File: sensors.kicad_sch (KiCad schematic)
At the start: 0 parts

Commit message: feat: setup encoder reading
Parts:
- added C30, C31: 10n, Capacitor_SMD:C_0603_1608Metric, symbol Device:C
- added C32, C33: 100n, Capacitor_SMD:C_0603_1608Metric, symbol Device:C
- added C34: 1n, Capacitor_SMD:C_0603_1608Metric, symbol Device:C
- added R13, R14: 120R, Resistor_SMD:R_0603_1608Metric, symbol Device:R
- added R15, R16, R17, R18: R, symbol Device:R
- added U2: ACS724LLCTR-10AB-T, Package_SO:SOIC-8_3.9x4.9mm_P1.27mm, symbol Sensor_Current:ACS724xLCTR-10AB
- added U3: UA9637A, Package_SO:SOIC-8_3.9x4.9mm_P1.27mm, symbol Eagle_Main:UA9637A
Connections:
- new net: C30.1, R13.1
- new net: R15.1, U3.2 (OUT1)
- new net: C31.1, R14.1
- new net: R16.1, U3.3 (OUT2)
- new net: U2.1 (IP+), U2.2 (IP+)
- new net: U2.3 (IP-), U2.4 (IP-)
- new net: C34.1, U2.6 (FILTER)
- new net +5V: C32.1, C33.1, U2.8 (VCC), U3.1 (VCC)
- new net GND: C32.2, C33.2, C34.2, R17.1, R18.2, U2.5 (GND), U3.4 (GND)
- new net M1_A: R15.2
- new net M1_A+: R13.2, U3.8 (IN1+)
- new net M1_A-: C30.2, U3.7 (IN1-)
- new net M1_B: R16.2, R17.2, R18.1
- new net M1_B+: R14.2, U3.6 (IN2+)
- new net M1_B-: C31.2, U3.5 (IN2-)
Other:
- note added: "MOTOR 1 - X axis"

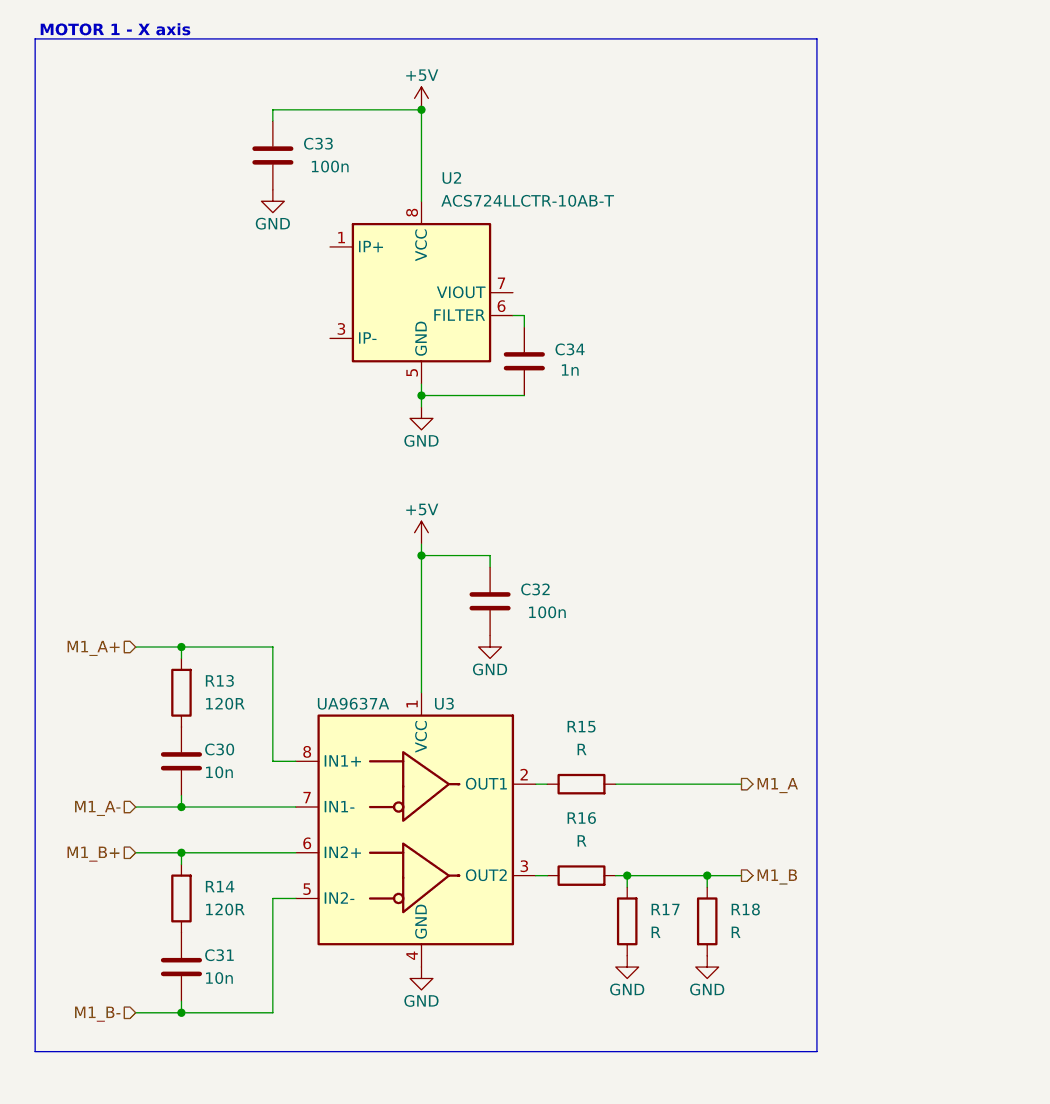
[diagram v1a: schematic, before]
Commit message: feat: RC filter on encoder data
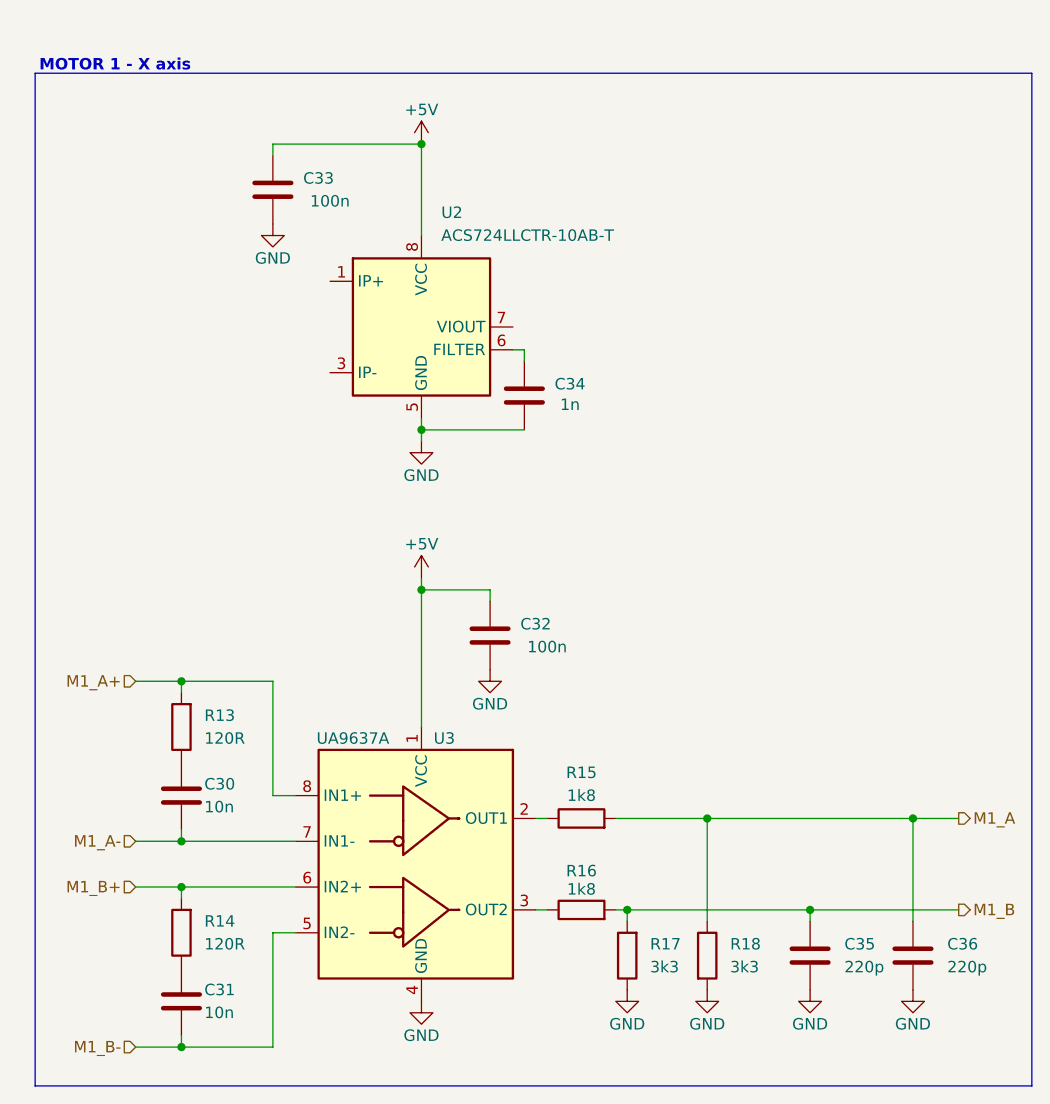
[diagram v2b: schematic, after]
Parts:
- added C35, C36: 220p, symbol Device:C
- R15, R16: value R -> 1k8
- R17, R18: value R -> 3k3
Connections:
- net GND: now also C35.2, C36.2
- net M1_A: now also R18.1, C36.1
- net M1_B: now also C35.1; no longer R18.1
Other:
- moved on the sheet: C30, C31, C32, C33, C34, R13, R14, R15, R16, R17, R18, U2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

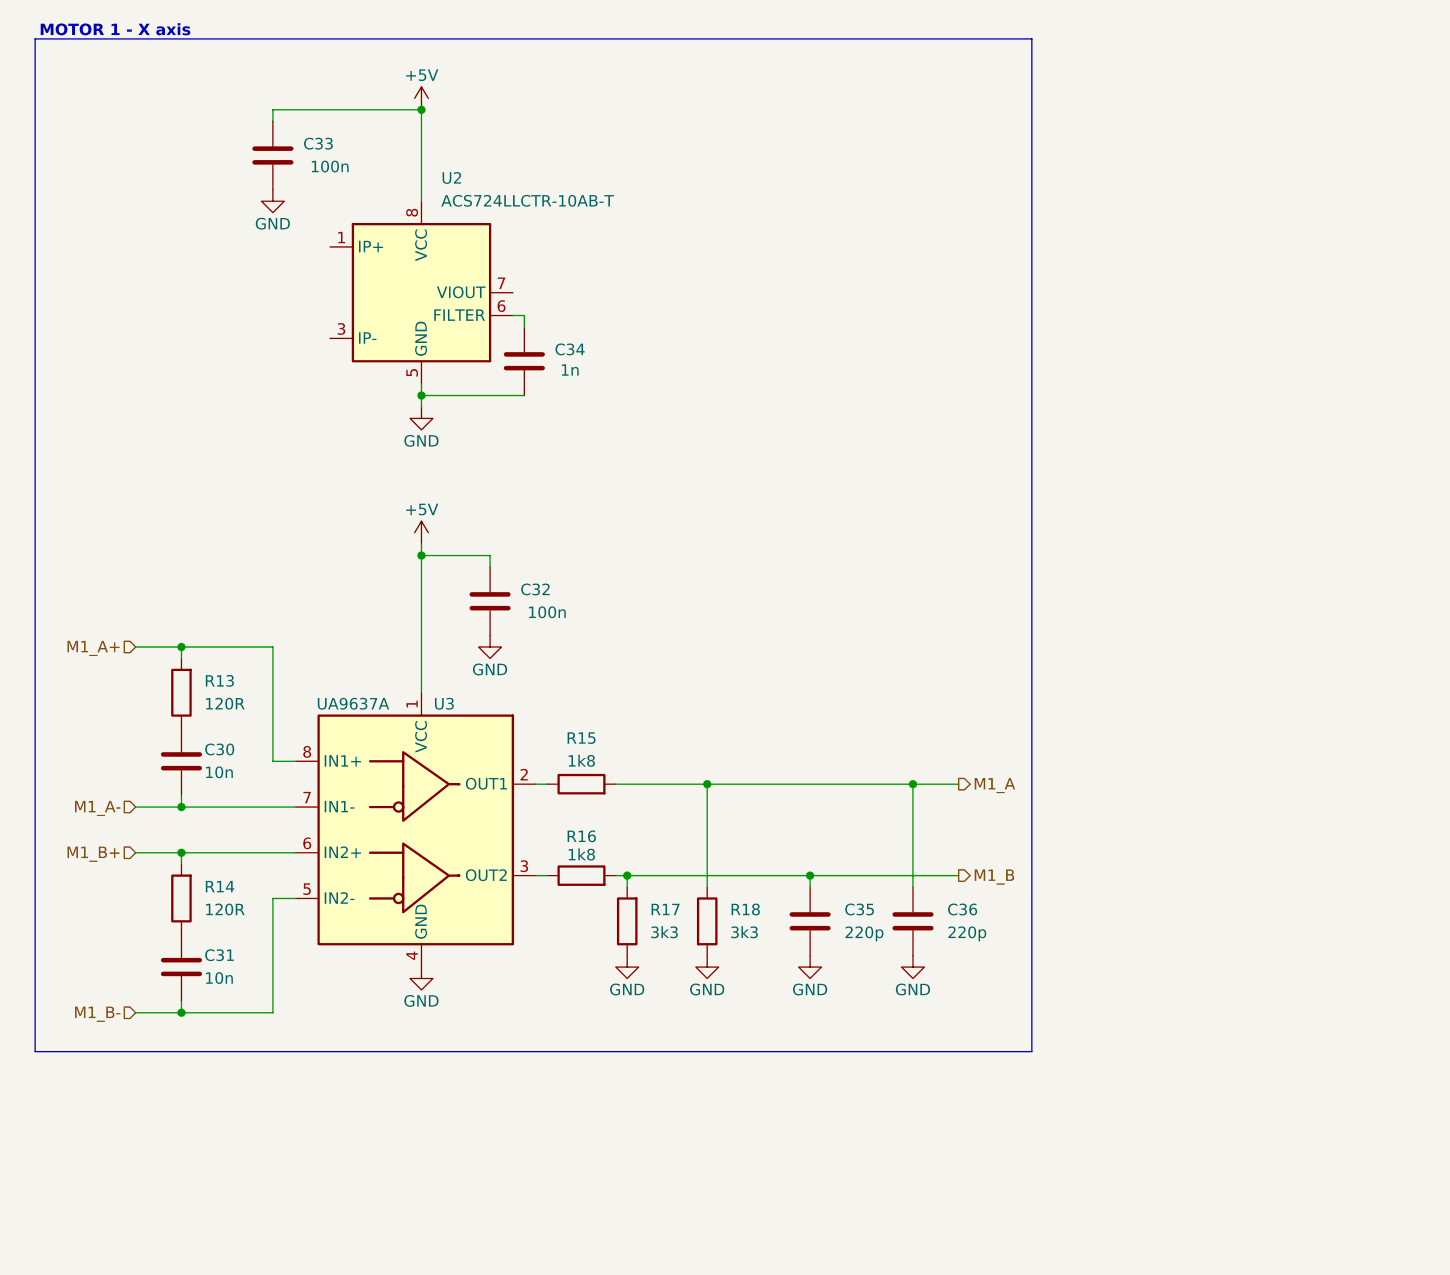
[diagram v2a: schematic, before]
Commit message: feat: voltage divider on UA96 inputs from new llinear encoder
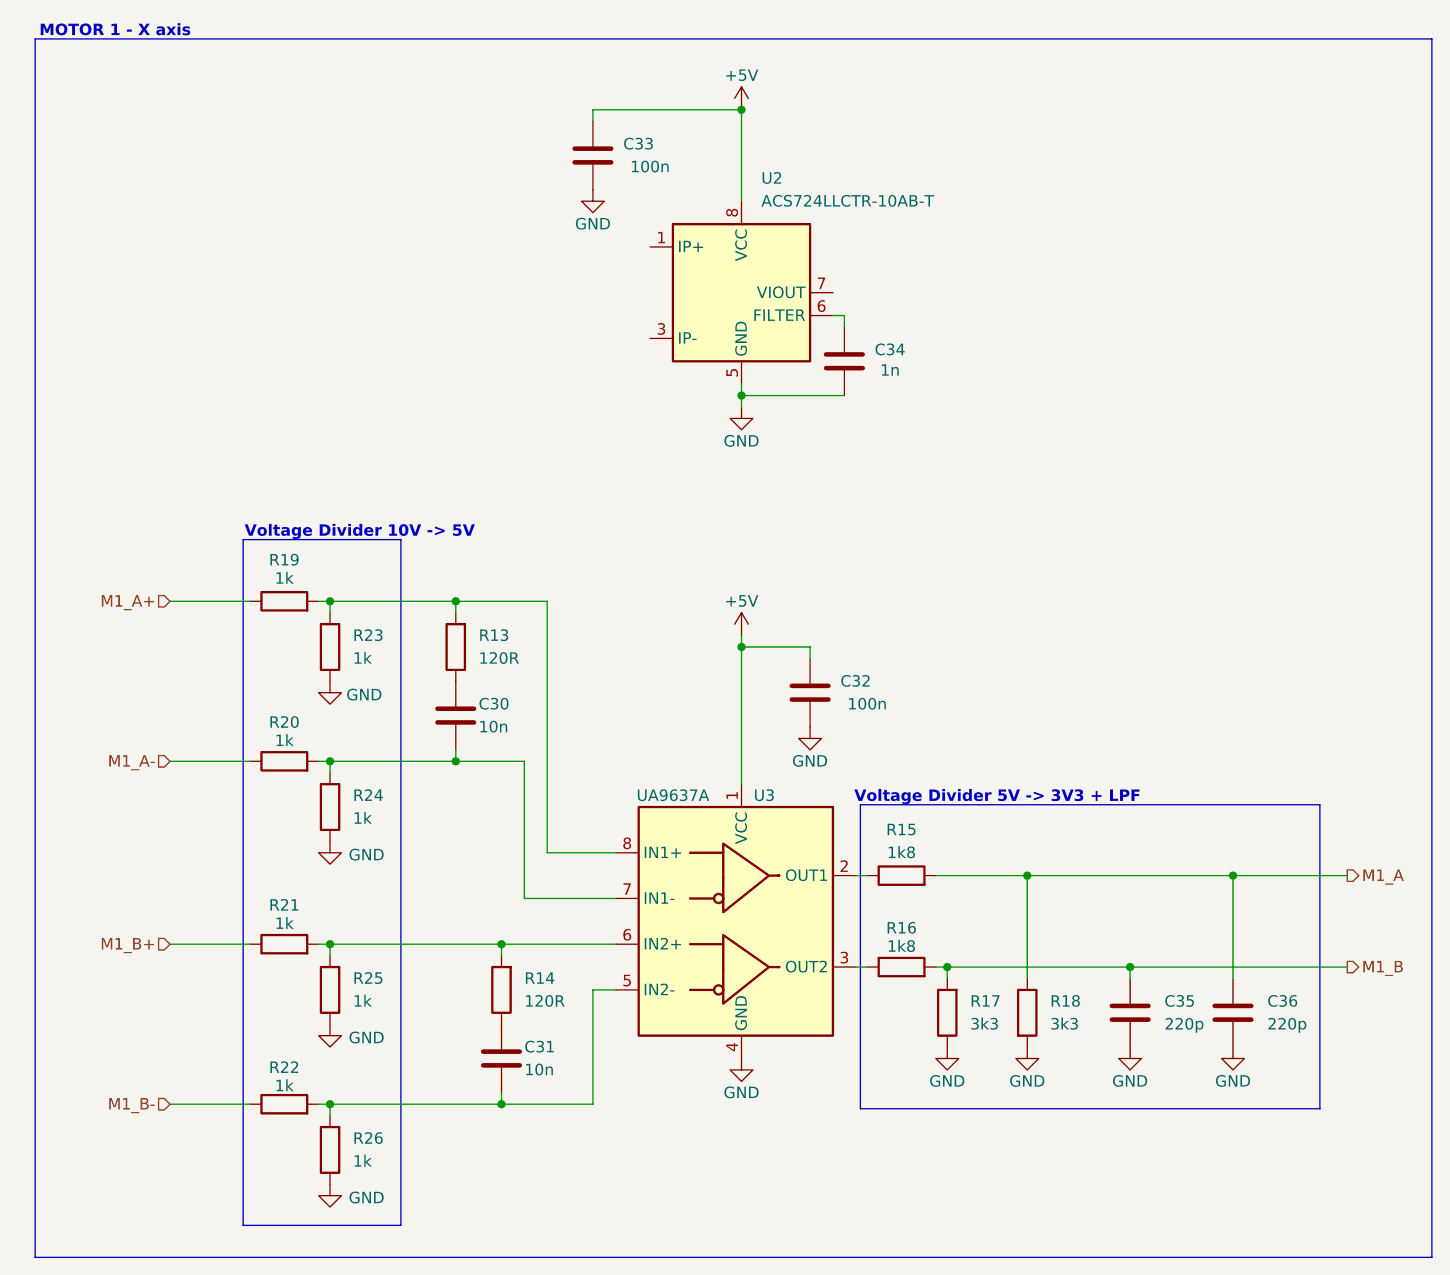
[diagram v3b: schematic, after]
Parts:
- added R19, R20, R21, R22, R23, R24, R25, R26: 1k, symbol Device:R
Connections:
- net GND: now also R23.1, R24.1, R25.1, R26.1
- net M1_A+: now also R19.1; no longer R13.2, U3.8 (IN1+)
- net M1_A-: now also R20.1; no longer C30.2, U3.7 (IN1-)
- net M1_B+: now also R21.1; no longer R14.2, U3.6 (IN2+)
- net M1_B-: now also R22.1; no longer C31.2, U3.5 (IN2-)
- new net: R13.2, R19.2, R23.2, U3.8 (IN1+)
- new net: R14.2, R21.2, R25.2, U3.6 (IN2+)
- new net: C30.2, R20.2, R24.2, U3.7 (IN1-)
- new net: C31.2, R22.2, R26.2, U3.5 (IN2-)
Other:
- note added: "Voltage Divider 10V -> 5V"
- note added: "Voltage Divider 5V -> 3V3 + LPF"
- moved on the sheet: C30, C31, C32, C33, C34, C35, C36, R13, R14, R15, R16, R17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
